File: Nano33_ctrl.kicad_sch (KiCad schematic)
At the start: 0 parts

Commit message: schematic fully captured
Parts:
- added C49 (x8): 10n, Capacitor_SMD:C_0805_2012Metric_Pad1.18x1.45mm_HandSolder, symbol Device:C_Small
- added C50 (x2): 100n, Capacitor_SMD:C_0805_2012Metric_Pad1.18x1.45mm_HandSolder, symbol Device:C_Small
- added C66: C_Small, symbol Device:C_Small
- added C68: 15u/35V, symbol Device:C_Small
- added C69: C_Polarized_Small, symbol Device:C_Polarized_Small
- added C71, C74: 10u, symbol Device:C_Small
- added C72: 100u/10V, symbol Device:C_Polarized_Small
- added D39, D40, D41, D43, D44: BAS16J, symbol Device:D_Small
- added D7: LED_Small, symbol Device:LED_Small
- added F1: 1A, symbol Device:Fuse_Small
- added FB1: FerriteBead_Small, symbol Device:FerriteBead_Small
- added J10, J11, J8: Conn_01x02, symbol Connector_Generic:Conn_01x02
- added J12: Arduino-NANO-33, Nano_33:NANO_33_Socket_Castell, symbol Arduino-nano-33:Arduino-NANO-33
- added J3: Power_In, symbol Connector_Generic:Conn_01x03
- added J4: Conn_Phoenix, symbol Connector_Generic:Conn_01x03
- added J5: To Display, symbol Connector_Generic:Conn_01x04
- added J6: To Protec_Brd encoder, symbol Connector_Generic:Conn_01x04
- added J7: To Protec_Brd, symbol Connector_Generic:Conn_02x05_Odd_Even
- added J9: To P.A., symbol Connector_Generic:Conn_01x05
- added R3: 1K, Resistor_SMD:R_0805_2012Metric_Pad1.20x1.40mm_HandSolder, symbol Device:R_Small
- added R32 (x6): 10k, Resistor_SMD:R_0805_2012Metric_Pad1.20x1.40mm_HandSolder, symbol Device:R_Small
- added U2: LM1117S-5.0, Package_TO_SOT_SMD:TO-263-3_TabPin2, symbol Regulator_Linear:LM1117S-5.0
- added U3: LM1117S-3.3, Package_TO_SOT_SMD:TO-263-3_TabPin2, symbol Regulator_Linear:LM1117S-3.3
- added U4: 74HCT04, symbol 74xx:74HCT04
- added U5, U6, U7: TPIC6595, symbol Interface_Expansion:TPIC6595
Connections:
- new net: D7.2 (A), R3.1
- new net: J12.16, R32.2, U4.5
- new net: C49.2, D39.1 (K), J8.1 (Pin_1)
- new net: D39.2 (A), J12.15, R32.2
- new net: D43.2 (A), J12.5
- new net: J12.10, R3.2
- new net: C66.1, F1.2, FB1.1
- new net: F1.1, J3.1 (Pin_1), J3.3 (Pin_3), J4.1 (Pin_1)
- new net: U4.6, U4.9
- new net: C49.2, D40.1 (K), J10.1 (Pin_1)
- new net: U4.11, U4.12
- new net: U4.2, U4.3
- new net: U4.4, U5.3 (SER_IN)
- new net: U5.18 (SER_OUT), U6.3 (SER_IN)
- new net: U6.18 (SER_OUT), U7.3 (SER_IN)
- new net +12V: C68.1, C69.1, C71.1, FB1.2, U2.3 (VI), U3.3 (VI)
- new net +3.3V: C49.1, C74.1, J12.17, R32.1, R32.1, R32.1, R32.1, R32.1, R32.1, U3.2 (VO)
- new net +5V: C49.1, C49.1, C50.1, C50.1, C72.1, J5.1 (Pin_1), U2.2 (VO), U4.14 (VCC), U5.2 (VCC), U5.8 (~{SRCLR}), U6.2 (VCC), U6.8 (~{SRCLR}), U7.2 (VCC), U7.8 (~{SRCLR})
- new net A6: J12.25, J9.1 (Pin_1)
- new net A7: J12.26, J9.2 (Pin_2)
- new net ANT1: U7.4 (DRAIN0)
- new net ANT2: U7.5 (DRAIN1)
- new net ANT3: U7.6 (DRAIN2)
- new net CAP1: U6.4 (DRAIN0)
- new net CAP2: U6.5 (DRAIN1)
- new net CAP3: U6.6 (DRAIN2)
- new net CAP4: U6.7 (DRAIN3)
- new net CAP5: U6.14 (DRAIN4)
- new net CAP6: U6.15 (DRAIN5)
- new net CAP7: U6.16 (DRAIN6)
- new net CAP8: U6.17 (DRAIN7)
- new net CAPOUT: U7.7 (DRAIN3)
- new net D2_A: D43.1 (K), J7.3 (Pin_3)
- new net D5_B: D41.1 (K), J7.4 (Pin_4)
- new net D8: J12.11, J7.5 (Pin_5)
- new net DATA: J12.14, R32.2, U4.1
- new net ENC1A: J12.21, J6.1 (Pin_1)
- new net ENC1B: J12.22, J6.2 (Pin_2)
- new net ENC_PB: J12.7, J6.3 (Pin_3)
- new net FWD: C49.1, J12.20, J7.8 (Pin_8)
- new net GND: C49.1, C49.1, C49.1, C49.2, C49.2, C49.2, C49.2, C49.2, C50.2, C50.2, C66.2, C68.2, C69.2, C71.2, C72.2, C74.2, D7.1 (K), J10.2 (Pin_2), J11.2 (Pin_2), J12.29, J12.4, J3.2 (Pin_2), J4.3 (Pin_3), J5.4 (Pin_4), J6.4 (Pin_4), J7.2 (Pin_2), J8.2 (Pin_2), J9.5 (Pin_5), U2.1 (GND), U3.1 (GND), U4.7 (GND), U5.1 (PGND), U5.10 (PGND), U5.11 (PGND), U5.19 (LGND), U5.20 (PGND), U5.9 (~{G}), U6.1 (PGND), U6.10 (PGND), U6.11 (PGND), U6.19 (LGND), U6.20 (PGND), U6.9 (~{G}), U7.1 (PGND), U7.10 (PGND), U7.11 (PGND), U7.19 (LGND), U7.20 (PGND), U7.9 (~{G})
- new net IND1: U5.4 (DRAIN0)
- new net IND2: U5.5 (DRAIN1)
- new net IND3: U5.6 (DRAIN2)
- new net IND4: U5.7 (DRAIN3)
- new net IND5: U5.14 (DRAIN4)
- new net IND6: U5.15 (DRAIN5)
- new net IND7: U5.16 (DRAIN6)
- new net IND8: U5.17 (DRAIN7)
- new net LOAD: J12.9, R32.2, U4.13
- new net PTT: D44.2 (A), J12.13, R32.2
- new net PTT_IN: C49.2, D44.1 (K), J11.1 (Pin_1), J7.10 (Pin_10), J9.4 (Pin_4)
- new net RCLK: U4.10, U5.12 (RCLK), U6.12 (RCLK), U7.12 (RCLK)
- new net RESET: J12.3, J7.1 (Pin_1)
- new net REV: C49.1, J12.19, J7.9 (Pin_9)
- new net RX: J12.2, J5.2 (Pin_2)
- new net SCL: J12.24, J7.6 (Pin_6)
- new net SDA: J12.23, J7.7 (Pin_7)
- new net SRCK: U4.8, U5.13 (SRCK), U6.13 (SRCK), U7.13 (SRCK)
- new net TUNE: D40.2 (A), J12.12, R32.2
- new net TUNE_PB: D41.2 (A), J12.8
- new net TX: J12.1, J5.3 (Pin_3)
- new net T/R_PTT: J12.6
- no-connect marks 0 -> 11
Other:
- note added: "?"
- note added: "Attention : Tous les connecteurs doivent être renumérotés pour rester cohérent avec les instructions de LA2NI et G8NJJ"
- note added: "PTT IN"
- note added: "STAND ALONE"
- note added: "TUNE"
- note added: "To Antenna switch"
- note added: "To transformer section"

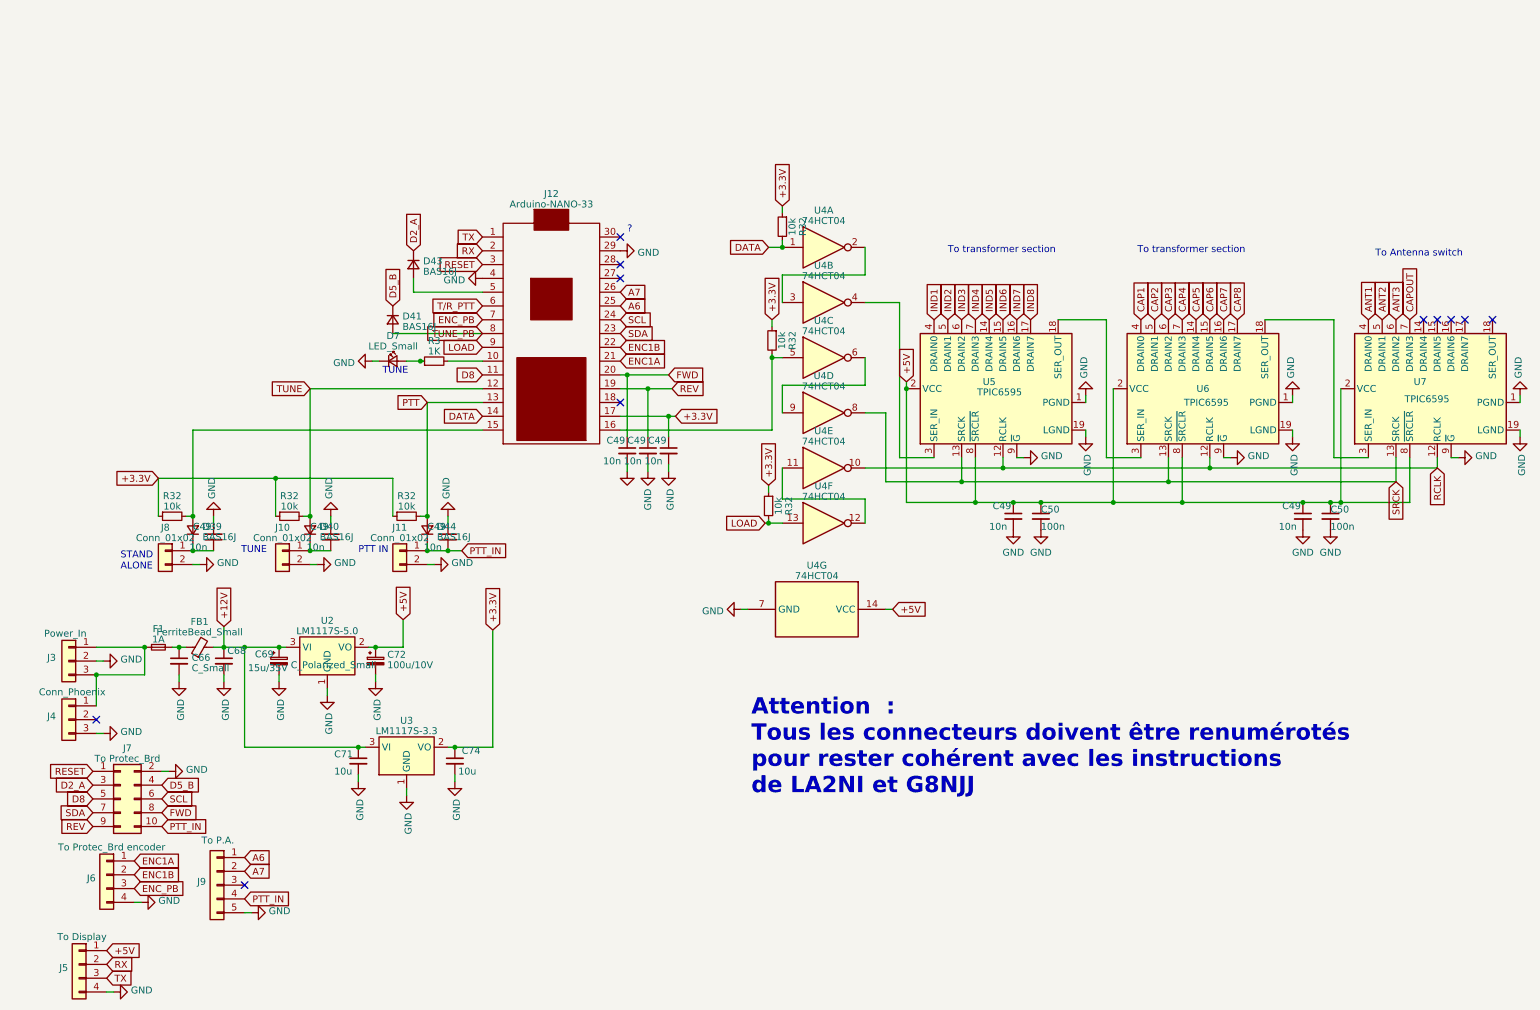
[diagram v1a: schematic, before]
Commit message: component-footprint association
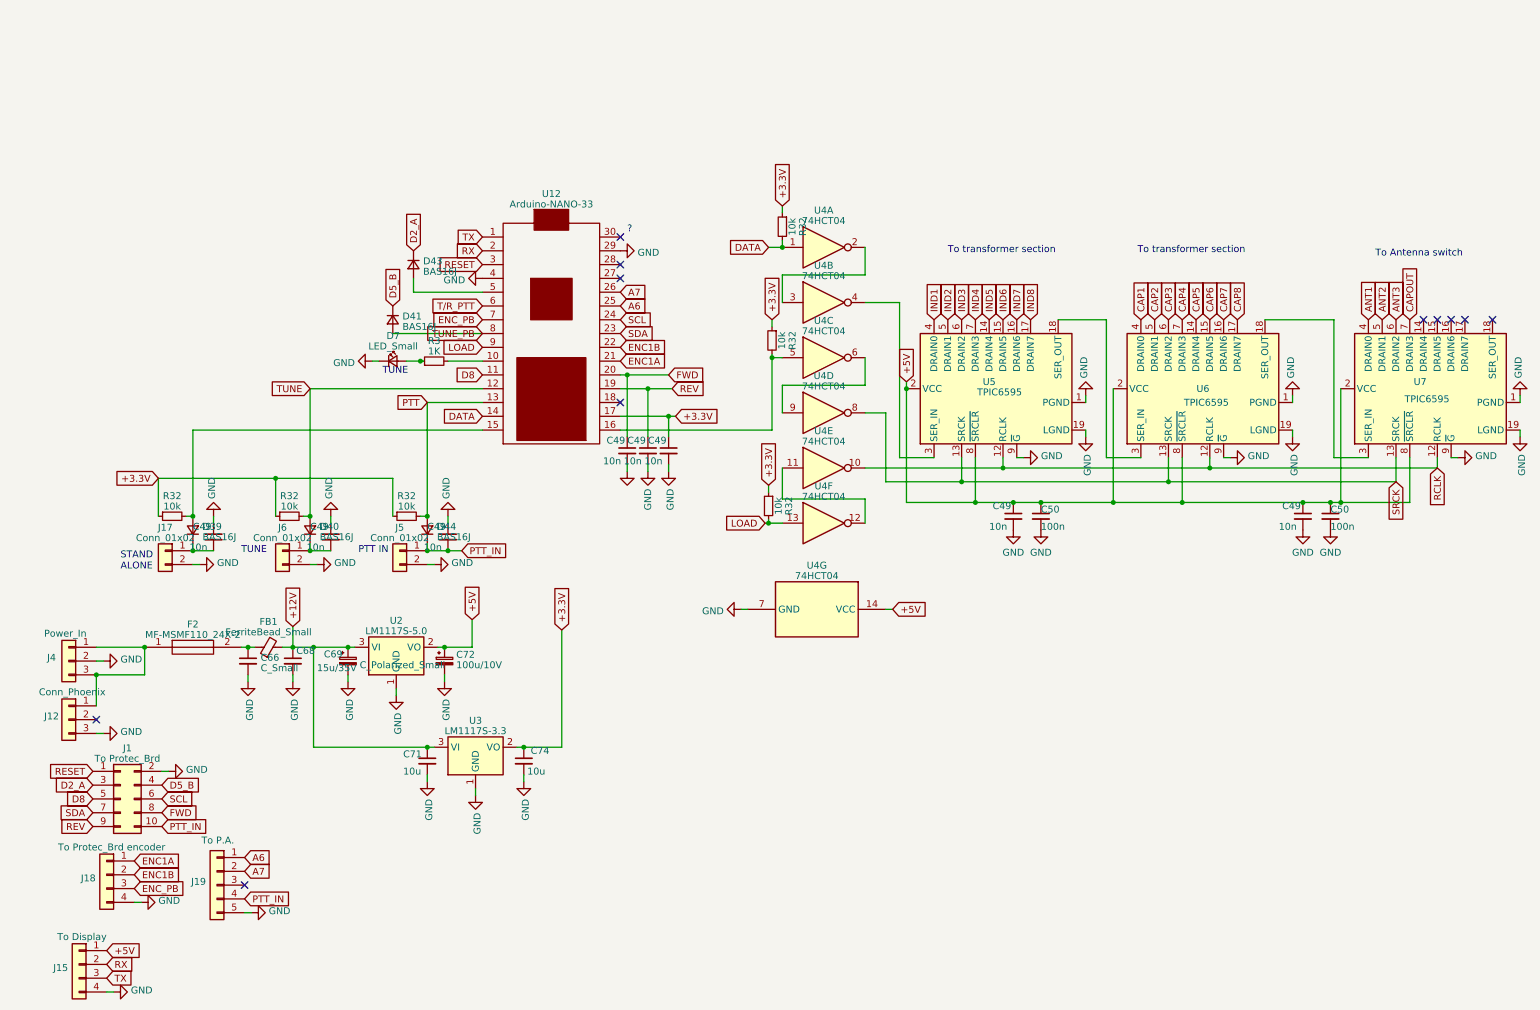
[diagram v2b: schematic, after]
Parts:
- removed F1: 1A, symbol Device:Fuse_Small
- added F2: MF-MSMF110_24X-2, MFMSMF11024X2:MFMSMF11024X2, symbol SamacSys_Parts:MF-MSMF110_24X-2
- D39, D40, D41, D43, D44: footprint (none) -> Diode_SMD:D_SOD-323_HandSoldering
- D7: footprint (none) -> LED_SMD:LED_1206_3216Metric_Pad1.42x1.75mm_HandSolder
- FB1: footprint (none) -> Inductor_SMD:L_2512_6332Metric_Pad1.52x3.35mm_HandSolder
- J1: renamed from J7; footprint (none) -> Connector_IDC:IDC-Header_2x05_P2.54mm_Vertical
- J15: renamed from J5; footprint (none) -> Connector_Molex:Molex_KK-254_AE-6410-04A_1x04_P2.54mm_Vertical
- J17: renamed from J8; footprint (none) -> Connector_Molex:Molex_KK-254_AE-6410-02A_1x02_P2.54mm_Vertical
- J18: renamed from J6; footprint (none) -> Connector_Molex:Molex_KK-254_AE-6410-04A_1x04_P2.54mm_Vertical
- J19: renamed from J9; footprint (none) -> Connector_Molex:Molex_KK-254_AE-6410-05A_1x05_P2.54mm_Vertical
- J4: renamed from J3; footprint (none) -> Connector_Molex:Molex_KK-254_AE-6410-03A_1x03_P2.54mm_Vertical
- J5: renamed from J11; footprint (none) -> Connector_Molex:Molex_KK-254_AE-6410-02A_1x02_P2.54mm_Vertical
- J6: renamed from J10; footprint (none) -> Connector_Molex:Molex_KK-254_AE-6410-02A_1x02_P2.54mm_Vertical
- U12: renamed from J12; footprint Nano_33:NANO_33_Socket_Castell -> Arduino-nano-33:NANO_33_Socket_Castell
- U4: footprint (none) -> Package_SO:SOIC-14_3.9x8.7mm_P1.27mm
- U5, U6, U7: footprint (none) -> Package_SO:SOIC-20W_7.5x12.8mm_P1.27mm
- renumbered J4 to J12
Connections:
- net at C66.1, FB1.1: now also F2.2
- net at J12.1 (Pin_1), J4.1 (Pin_1), J4.3 (Pin_3): now also F2.1
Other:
- note removed: "Attention : Tous les connecteurs doivent être renumérotés pour rester cohérent avec les instructions de LA2NI et G8NJJ"
- moved on the sheet: C66, C68, C69, C71, C72, C74, FB1, U2, U3

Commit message: dual footprint for serial eprom
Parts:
- added C101: 10u/35V, Capacitor_Tantalum_SMD:CP_EIA-6032-28_Kemet-C_Pad2.25x2.35mm_HandSolder, symbol Device:C_Small
- added R32 (x2): 10k, Resistor_SMD:R_0805_2012Metric_Pad1.20x1.40mm_HandSolder, symbol Device:R_Small
- added U8: 24FC1025-I_SN, Package_SO:SOIC-8-N7_3.9x4.9mm_P1.27mm, symbol 24FC1025:24FC1025-I_SN
- added U9: 24FC1025-I_SN, Package_DIP:DIP-8_W8.89mm_SMDSocket_LongPads, symbol 24FC1025:24FC1025-I_SN
- C66: value C_Small -> 10u/35V; footprint (none) -> Capacitor_Tantalum_SMD:CP_EIA-6032-28_Kemet-C_Pad2.25x2.35mm_HandSolder
- C68: value 15u/35V -> 10u/35V; footprint (none) -> Capacitor_Tantalum_SMD:CP_EIA-6032-28_Kemet-C_Pad2.25x2.35mm_HandSolder
- C69: value C_Polarized_Small -> 10u/35V; footprint (none) -> Capacitor_Tantalum_SMD:CP_EIA-6032-28_Kemet-C_Pad2.25x2.35mm_HandSolder
- C71, C74: footprint (none) -> Capacitor_SMD:C_0805_2012Metric_Pad1.18x1.45mm_HandSolder
- C72: footprint (none) -> Capacitor_Tantalum_SMD:CP_EIA-7132-28_AVX-C_Pad2.72x3.50mm_HandSolder
- J12: value Conn_Phoenix -> MKDSP 1.5/ 2-5.08
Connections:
- net +3.3V: now also R32.2, R32.2, U8.8 (VCC), U9.8 (VCC)
- net GND: now also C101.2, U8.2 (A1), U8.3 (A2), U8.4 (VSS), U8.7 (WP), U9.2 (A1), U9.3 (A2), U9.4 (VSS), U9.7 (WP)
- net SCL: now also R32.1, U8.6 (SCL), U9.6 (SCL)
- net SDA: now also R32.1, U8.5 (SDA), U9.5 (SDA)
- net at F2.1, J12.1 (Pin_1), J4.1 (Pin_1)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: now also C101.1
- no-connect marks 11 -> 14
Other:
- note added: "Alternate footprint"

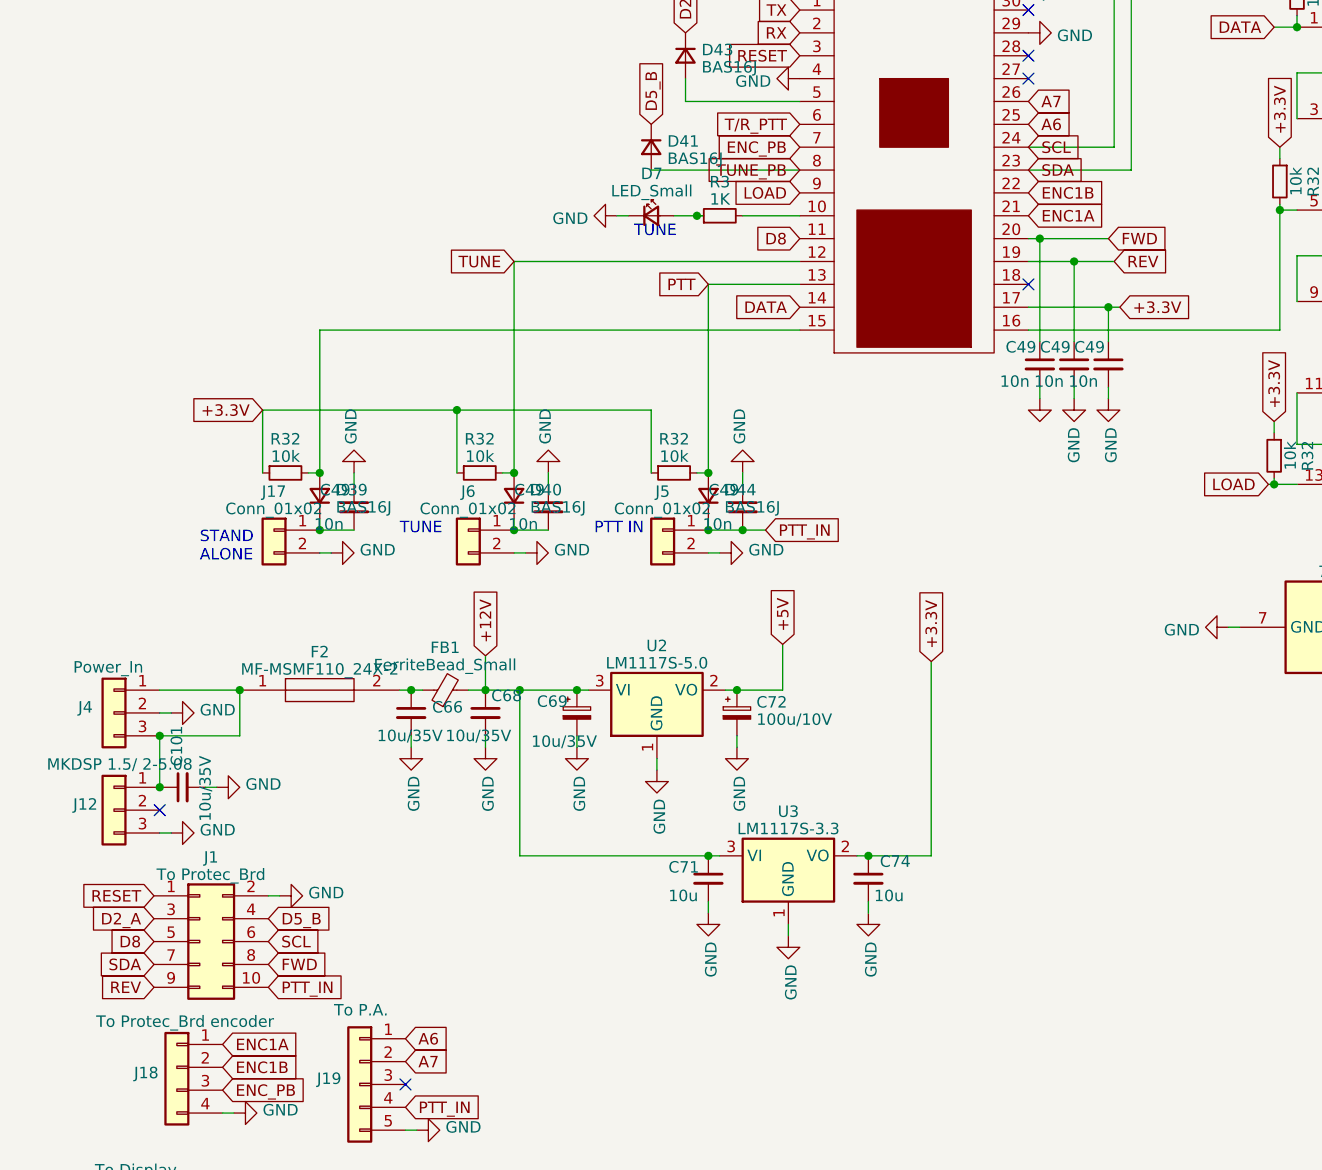
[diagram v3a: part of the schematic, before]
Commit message: all component sourced, all 3D object configured
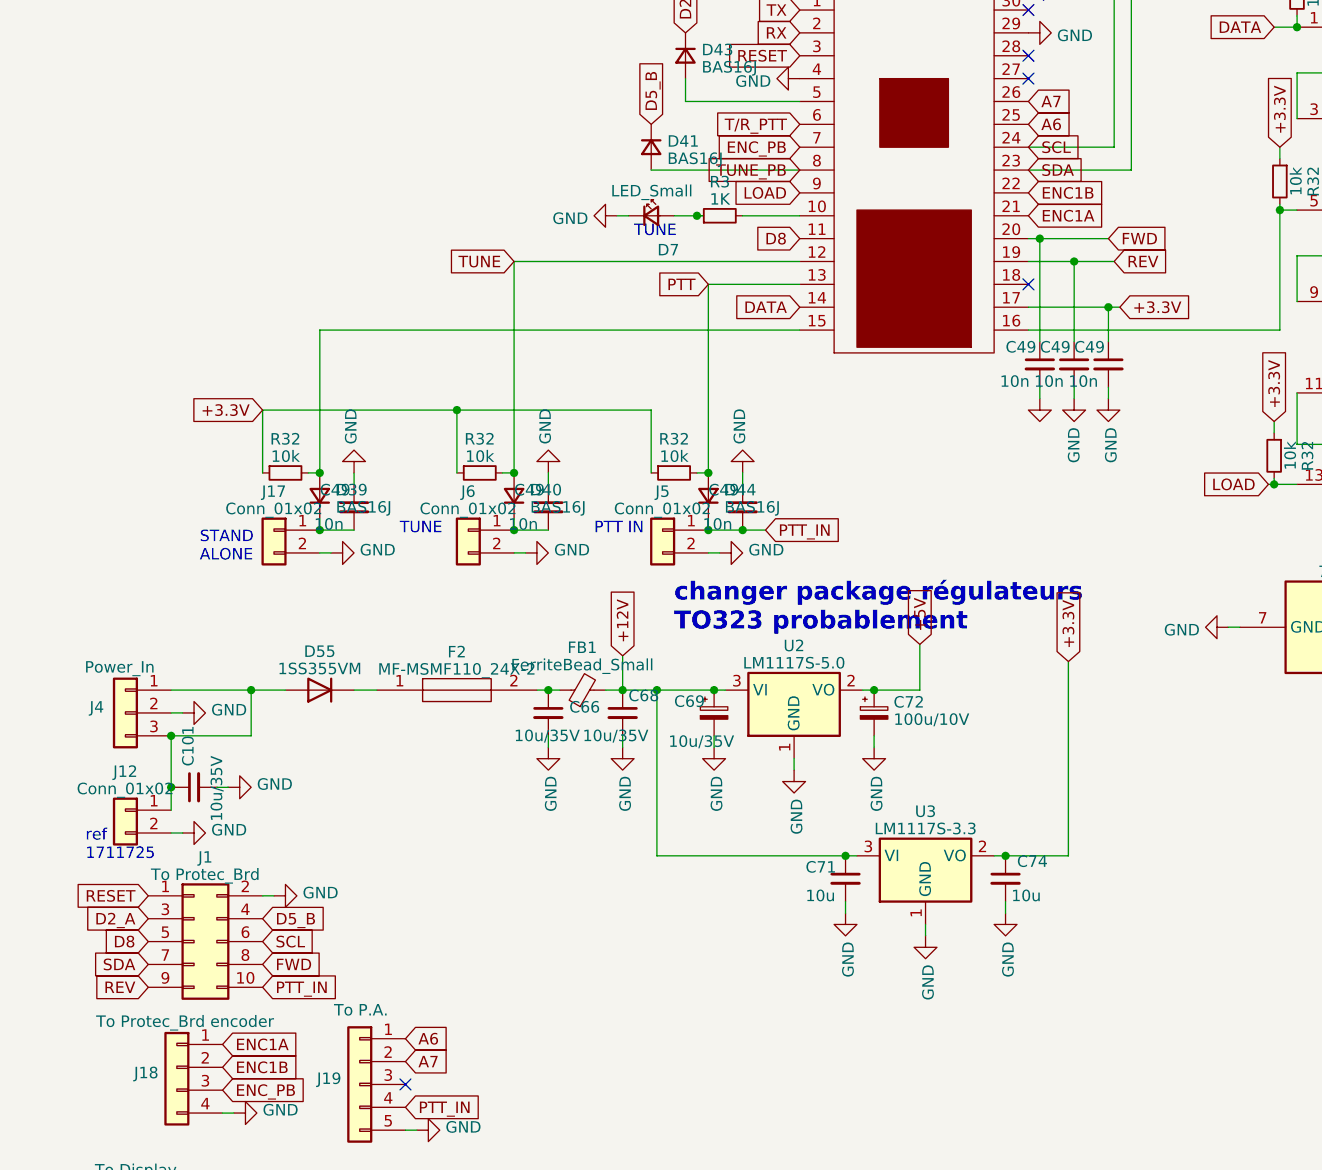
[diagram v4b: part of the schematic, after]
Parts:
- removed J12: MKDSP 1.5/ 2-5.08, symbol Connector_Generic:Conn_01x03
- added D55: 1SS355VM, Diode_SMD:D_1210_3225Metric_Pad1.42x2.65mm_HandSolder, symbol Diode:1SS355VM
- added J12: Conn_01x02, Connector_Phoenix_1711725:1711725, symbol Connector_Generic:Conn_01x02
- U2, U3: footprint Package_TO_SOT_SMD:TO-263-3_TabPin2 -> Package_TO_SOT_SMD:SOT-223-3_TabPin2
- U8: footprint Package_SO:SOIC-8-N7_3.9x4.9mm_P1.27mm -> Package_SO:SOIC-8_3.9x4.9mm_P1.27mm
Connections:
- net GND: now also J12.2 (Pin_2)
- net at C101.1, J4.1 (Pin_1), J4.3 (Pin_3): now also D55.2 (A), J12.1 (Pin_1); no longer F2.1
- new net: D55.1 (K), F2.1
- no-connect marks 14 -> 13
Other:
- note added: "changer package régulateurs TO323 probablement"
- note added: "ref 1711725"
- moved on the sheet: C101, C66, C68, C69, C71, C72, C74, F2, FB1, J1, J4, U2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
